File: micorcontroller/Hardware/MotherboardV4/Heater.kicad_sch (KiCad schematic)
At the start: 48 parts, among them IC1 ITS4200S-ME-O, IC10 ITS4200S-ME-O, IC11 ITS4200S-ME-O, IC4 ITS4200S-ME-O, IC6 ITS4200S-ME-O, IC7 ITS4200S-ME-O, IC8 ITS4200S-ME-O, IC9 ITS4200S-ME-O

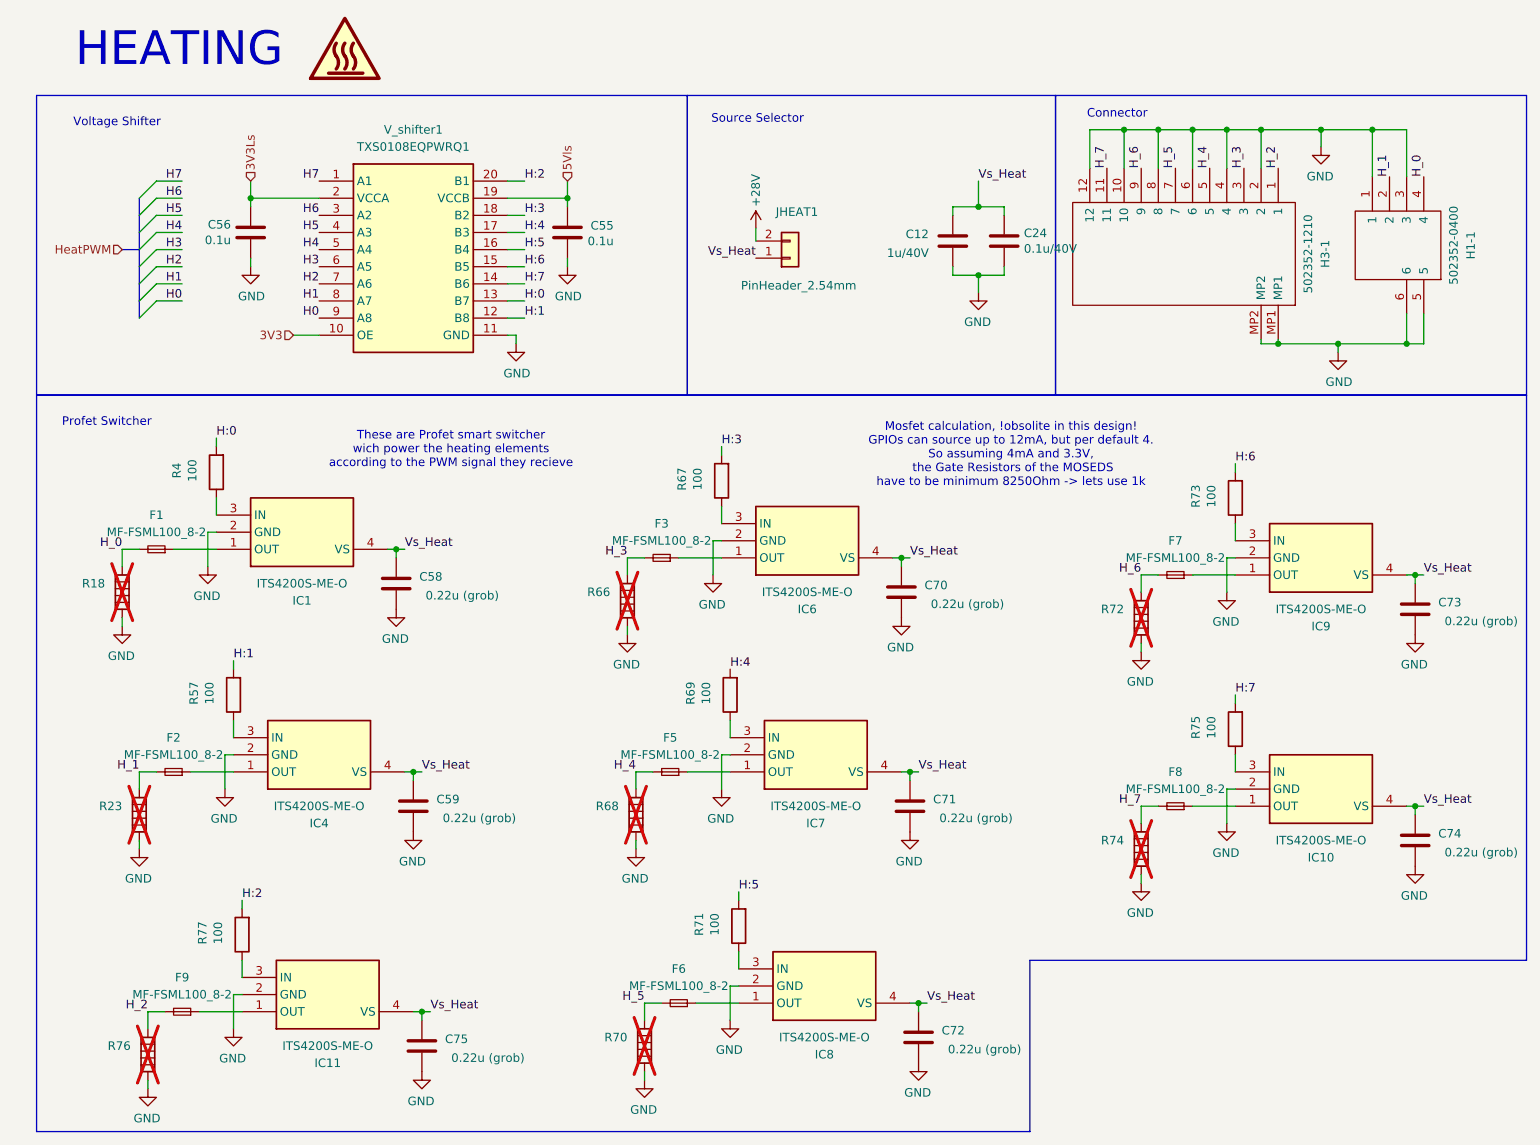
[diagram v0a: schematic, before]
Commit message: added NTC calculation
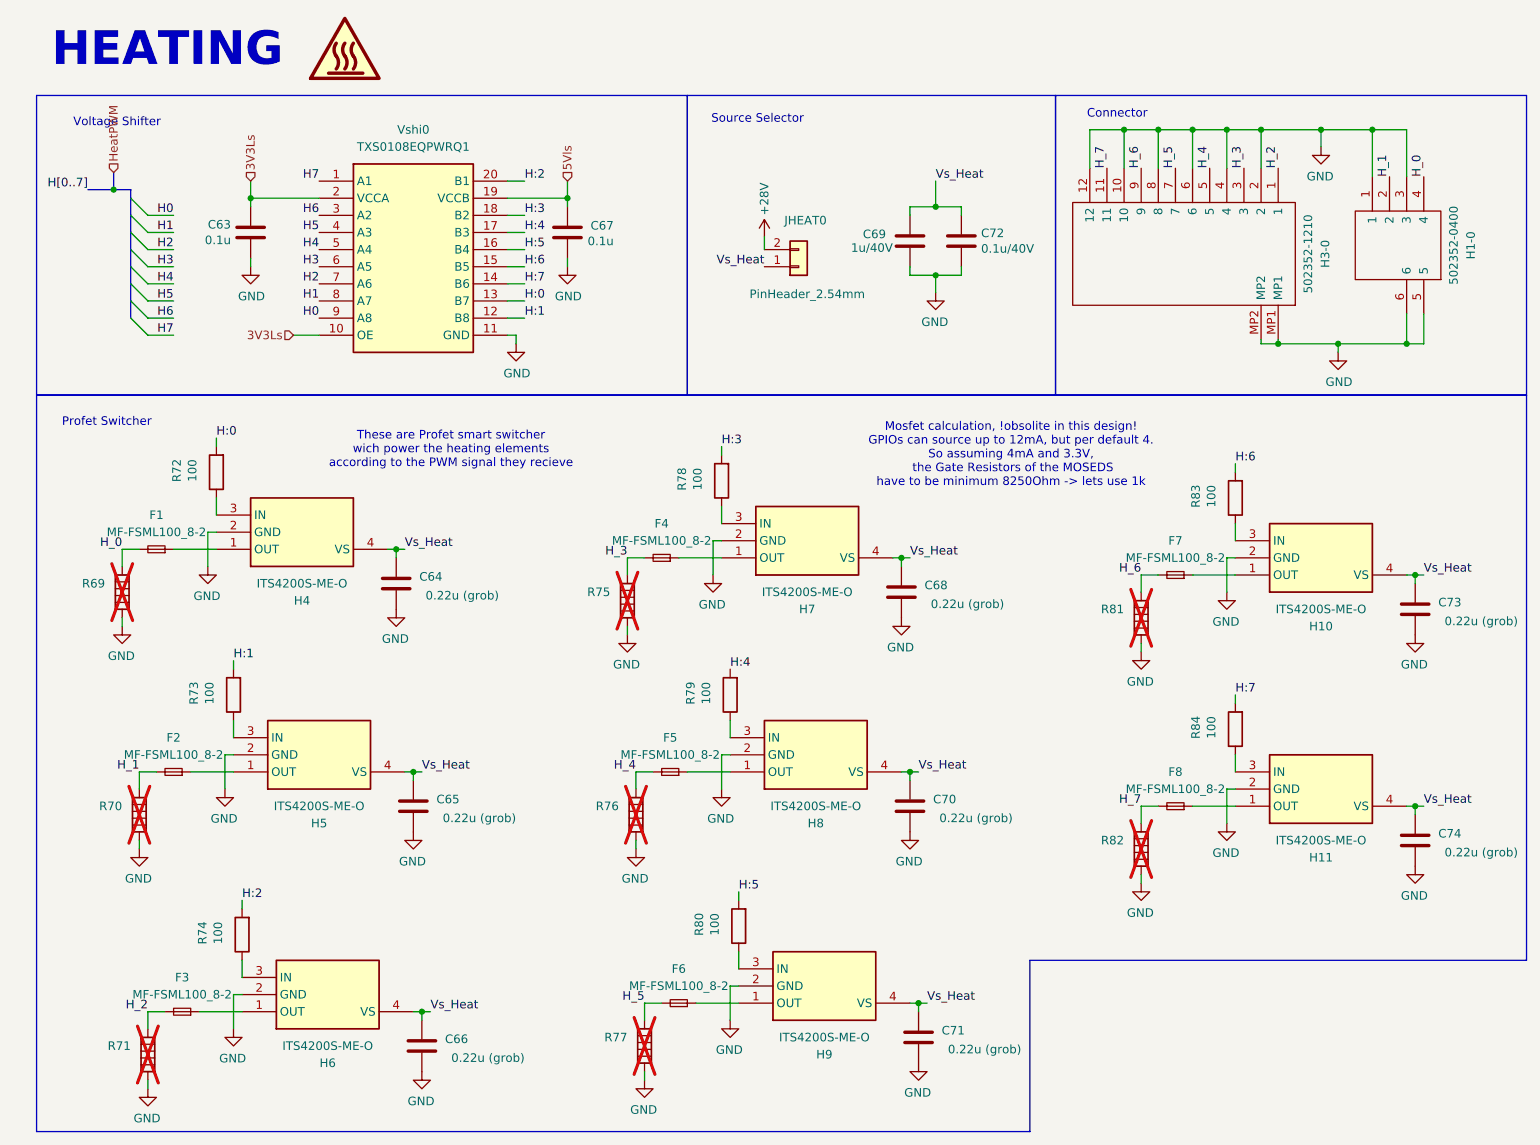
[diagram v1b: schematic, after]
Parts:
- renumbered C56 to C63, C58 to C64, C59 to C65, C75 to C66, C55 to C67, C70 to C68, C12 to C69, C71 to C70, C72 to C71, C24 to C72, F9 to F3, F3 to F4, H1-1 to H1-0, IC9 to H10, IC10 to H11, H3-1 to H3-0, IC1 to H4, IC4 to H5, IC11 to H6, IC6 to H7, IC7 to H8, IC8 to H9, JHEAT1 to JHEAT0, R18 to R69, R23 to R70, R76 to R71, R4 to R72, R57 to R73, R77 to R74, R66 to R75, R68 to R76, R70 to R77, R67 to R78, R69 to R79, R71 to R80, R72 to R81, R74 to R82, R73 to R83, R75 to R84, V_shifter1 to Vshi0
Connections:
- net 3V3 is gone; now on net 3V3Ls: Vshi0.10 (OE)
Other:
- moved on the sheet: C69, C72, JHEAT0

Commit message: added a serial command field for easy debugging
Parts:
- C69: value 1u/40V -> 1u/30V DNP
- C72: value 0.1u/40V -> 0.1u/30V DNP; footprint Capacitor_SMD:C_0402_1005Metric_Pad0.74x0.62mm_HandSolder -> Capacitor_SMD:C_0805_2012Metric_Pad1.18x1.45mm_HandSolder
- renumbered H4 to H0, H5 to H1, H6 to H2, H7 to H3, H8 to H4, H9 to H5, H10 to H6, H11 to H7
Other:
- moved on the sheet: JHEAT0
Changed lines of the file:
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@@
 	)
 	(junction
-		(at 160.02 55.88)
-		(diameter 0)
-		(color 0 0 0 0)
-	)
-	(junction
 		(at 156.21 129.54)
 		(diameter 0)
@@
 	)
 	(junction
+		(at 160.02 58.42)
+		(diameter 0)
+		(color 0 0 0 0)
+	)
+	(junction
 		(at 229.87 66.04)
 		(diameter 0)
@@
 	(wire
 		(pts
-			(xy 160.02 55.88) (xy 156.21 55.88)
+			(xy 160.02 58.42) (xy 156.21 58.42)
 		)
 		(stroke
@@
 	(wire
 		(pts
-			(xy 160.02 58.42) (xy 160.02 55.88)
-		)
-		(stroke
-			(width 0)
-			(type default)
-		)
-	)
-	(wire
-		(pts
 			(xy 64.77 64.77) (xy 68.58 64.77)
 		)
@@
 	(wire
 		(pts
-			(xy 163.83 55.88) (xy 163.83 54.61)
+			(xy 163.83 58.42) (xy 163.83 54.61)
 		)
 		(stroke
@@
 	(wire
 		(pts
-			(xy 163.83 55.88) (xy 160.02 55.88)
+			(xy 163.83 58.42) (xy 160.02 58.42)
 		)
 		(stroke
@@
 	(wire
 		(pts
-			(xy 134.62 50.165) (xy 134.62 52.07)
+			(xy 132.08 47.625) (xy 132.08 49.53)
 		)
 		(stroke
@@
 	(wire
 		(pts
+			(xy 160.02 58.42) (xy 160.02 60.96)
+		)
+		(stroke
+			(width 0)
+			(type default)
+		)
+	)
+	(wire
+		(pts
 			(xy 43.18 176.53) (xy 43.18 175.26)
 		)
@@
 	(wire
 		(pts
-			(xy 156.21 55.88) (xy 156.21 54.61)
+			(xy 156.21 58.42) (xy 156.21 54.61)
 		)
 		(stroke
@@
 	)
 	(label "Vs_Heat"
-		(at 134.62 54.61 180)
+		(at 132.08 52.07 180)
 		(fields_autoplaced yes)
 		(effects
@@
 		(on_board yes)
 		(dnp no)
-		(property "Reference" "H11"
+		(property "Reference" "H7"
 			(at 217.17 142.24 0)
 			(effects
@@
 			(project "BalloonMotherboardV4"
 				(path "/a70d325c-f83f-4714-a2b6-4ef8919d016e/ef45ab9a-94f0-47f5-90d7-9f2f46e21e77"
-					(reference "H11")
+					(reference "H7")
 					(unit 1)
 				)
@@
 		(on_board yes)
 		(dnp no)
-		(property "Reference" "H6"
+		(property "Reference" "H2"
 			(at 69.85 172.72 0)
 			(effects
@@
 			(project "BalloonMotherboardV4"
 				(path "/a70d325c-f83f-4714-a2b6-4ef8919d016e/ef45ab9a-94f0-47f5-90d7-9f2f46e21e77"
-					(reference "H6")
+					(reference "H2")
 					(unit 1)
 				)
@@
 		(dnp no)
 		(property "Reference" "C69"
-			(at 152.654 49.784 0)
+			(at 155.956 48.514 0)
 			(effects
 				(font
@@
 			)
 		)
-		(property "Value" "1u/40V"
-			(at 153.67 51.816 0)
+		(property "Value" "1u/30V DNP"
+			(at 160.782 53.848 0)
 			(effects
 				(font
@@
 		(on_board yes)
 		(dnp no)
-		(property "Reference" "H10"
+		(property "Reference" "H6"
 			(at 217.17 107.95 0)
 			(effects
@@
 			(project "BalloonMotherboardV4"
 				(path "/a70d325c-f83f-4714-a2b6-4ef8919d016e/ef45ab9a-94f0-47f5-90d7-9f2f46e21e77"
-					(reference "H10")
+					(reference "H6")
 					(unit 1)
 				)
@@
 		(on_board yes)
 		(dnp no)
-		(property "Reference" "H4"
+		(property "Reference" "H0"
 			(at 66.04 104.14 0)
 			(effects
@@
 			(project "BalloonMotherboardV4"
 				(path "/a70d325c-f83f-4714-a2b6-4ef8919d016e/ef45ab9a-94f0-47f5-90d7-9f2f46e21e77"
-					(reference "H4")
+					(reference "H0")
 					(unit 1)
 				)
@@
 		(on_board yes)
 		(dnp no)
-		(property "Reference" "H8"
+		(property "Reference" "H4"
 			(at 142.24 137.16 0)
 			(effects
@@
 			(project "BalloonMotherboardV4"
 				(path "/a70d325c-f83f-4714-a2b6-4ef8919d016e/ef45ab9a-94f0-47f5-90d7-9f2f46e21e77"
-					(reference "H8")
+					(reference "H4")
 					(unit 1)
 				)
@@
 		(on_board yes)
 		(dnp no)
-		(property "Reference" "H9"
+		(property "Reference" "H5"
 			(at 143.51 171.45 0)
 			(effects
@@
 			(project "BalloonMotherboardV4"
 				(path "/a70d325c-f83f-4714-a2b6-4ef8919d016e/ef45ab9a-94f0-47f5-90d7-9f2f46e21e77"
-					(reference "H9")
+					(reference "H5")
 					(unit 1)
 				)
@@
 		(on_board yes)
 		(dnp no)
-		(property "Reference" "H7"
+		(property "Reference" "H3"
 			(at 140.97 105.41 0)
 			(effects
@@
 			(project "BalloonMotherboardV4"
 				(path "/a70d325c-f83f-4714-a2b6-4ef8919d016e/ef45ab9a-94f0-47f5-90d7-9f2f46e21e77"
-					(reference "H7")
+					(reference "H3")
 					(unit 1)
 				)
@@
 	(symbol
 		(lib_id "Connector_Generic:Conn_01x02")
-		(at 139.7 54.61 0)
+		(at 137.16 52.07 0)
 		(mirror x)
 		(unit 1)
@@
 		(dnp no)
 		(property "Reference" "JHEAT0"
-			(at 140.716 47.752 0)
+			(at 138.176 45.212 0)
 			(effects
 				(font
@@
 		)
 		(property "Value" "PinHeader_2.54mm"
-			(at 140.97 58.674 0)
+			(at 138.43 56.134 0)
 			(effects
 				(font
@@
 		)
 		(property "Footprint" "Connector_PinHeader_2.54mm:PinHeader_1x02_P2.54mm_Vertical"
-			(at 139.7 54.61 0)
+			(at 137.16 52.07 0)
 			(effects
 				(font
@@
 		)
 		(property "Datasheet" "~"
-			(at 139.7 54.61 0)
+			(at 137.16 52.07 0)
 			(effects
 				(font
@@
 		)
 		(property "Description" "Generic connector, single row, 01x02, script generated (kicad-library-utils/schlib/autogen/connector/)"
-			(at 139.7 54.61 0)
+			(at 137.16 52.07 0)
 			(effects
 				(font
@@
 		(dnp no)
 		(property "Reference" "C72"
-			(at 166.751 49.6316 0)
+			(at 164.846 48.26 0)
 			(effects
 				(font
@@
 			)
 		)
-		(property "Value" "0.1u/40V"
-			(at 166.751 51.943 0)
+		(property "Value" "0.1u/30V DNP"
+			(at 159.258 56.388 0)
 			(effects
 				(font
@@
 			)
 		)
-		(property "Footprint" "Capacitor_SMD:C_0402_1005Metric_Pad0.74x0.62mm_HandSolder"
+		(property "Footprint" "Capacitor_SMD:C_0805_2012Metric_Pad1.18x1.45mm_HandSolder"
 			(at 164.7952 54.61 0)
 			(effects
@@
 		(on_board yes)
 		(dnp no)
-		(property "Reference" "H5"
+		(property "Reference" "H1"
 			(at 68.58 137.16 0)
 			(effects
@@
 			(project "BalloonMotherboardV4"
 				(path "/a70d325c-f83f-4714-a2b6-4ef8919d016e/ef45ab9a-94f0-47f5-90d7-9f2f46e21e77"
-					(reference "H5")
+					(reference "H1")
 					(unit 1)
 				)
@@
 	(symbol
 		(lib_id "power:+28V")
-		(at 134.62 50.165 0)
+		(at 132.08 47.625 0)
 		(unit 1)
 		(exclude_from_sim no)
@@
 		(fields_autoplaced yes)
 		(property "Reference" "#PWR0112"
-			(at 134.62 53.975 0)
+			(at 132.08 51.435 0)
 			(effects
 				(font
@@
 		)
 		(property "Value" "+28V"
-			(at 134.62 46.99 90)
+			(at 132.08 44.45 90)
 			(effects
 				(font
@@
 		)
 		(property "Footprint" ""
-			(at 140.97 48.895 0)
+			(at 138.43 46.355 0)
 			(effects
 				(font
@@
 		)
 		(property "Datasheet" ""
-			(at 140.97 48.895 0)
+			(at 138.43 46.355 0)
 			(effects
 				(font
@@
 		)
 		(property "Description" "Power symbol creates a global label with name \"+28V\""
-			(at 134.62 50.165 0)
+			(at 132.08 47.625 0)
 			(effects
 				(font
@@
 	(symbol
 		(lib_id "power:GND")
-		(at 160.02 58.42 0)
+		(at 160.02 60.96 0)
 		(mirror y)
 		(unit 1)
@@
 		(dnp no)
 		(property "Reference" "#PWR0116"
-			(at 160.02 64.77 0)
+			(at 160.02 67.31 0)
 			(effects
 				(font
@@
 		)
 		(property "Value" "GND"
-			(at 159.893 62.8142 0)
+			(at 159.893 65.3542 0)
 			(effects
 				(font
@@
 		)
 		(property "Footprint" ""
-			(at 160.02 58.42 0)
+			(at 160.02 60.96 0)
 			(effects
 				(font
@@
 		)
 		(property "Datasheet" ""
-			(at 160.02 58.42 0)
+			(at 160.02 60.96 0)
 			(effects
 				(font
@@
 		)
 		(property "Description" "Power symbol creates a global label with name \"GND\" , ground"
-			(at 160.02 58.42 0)
+			(at 160.02 60.96 0)
 			(effects
 				(font

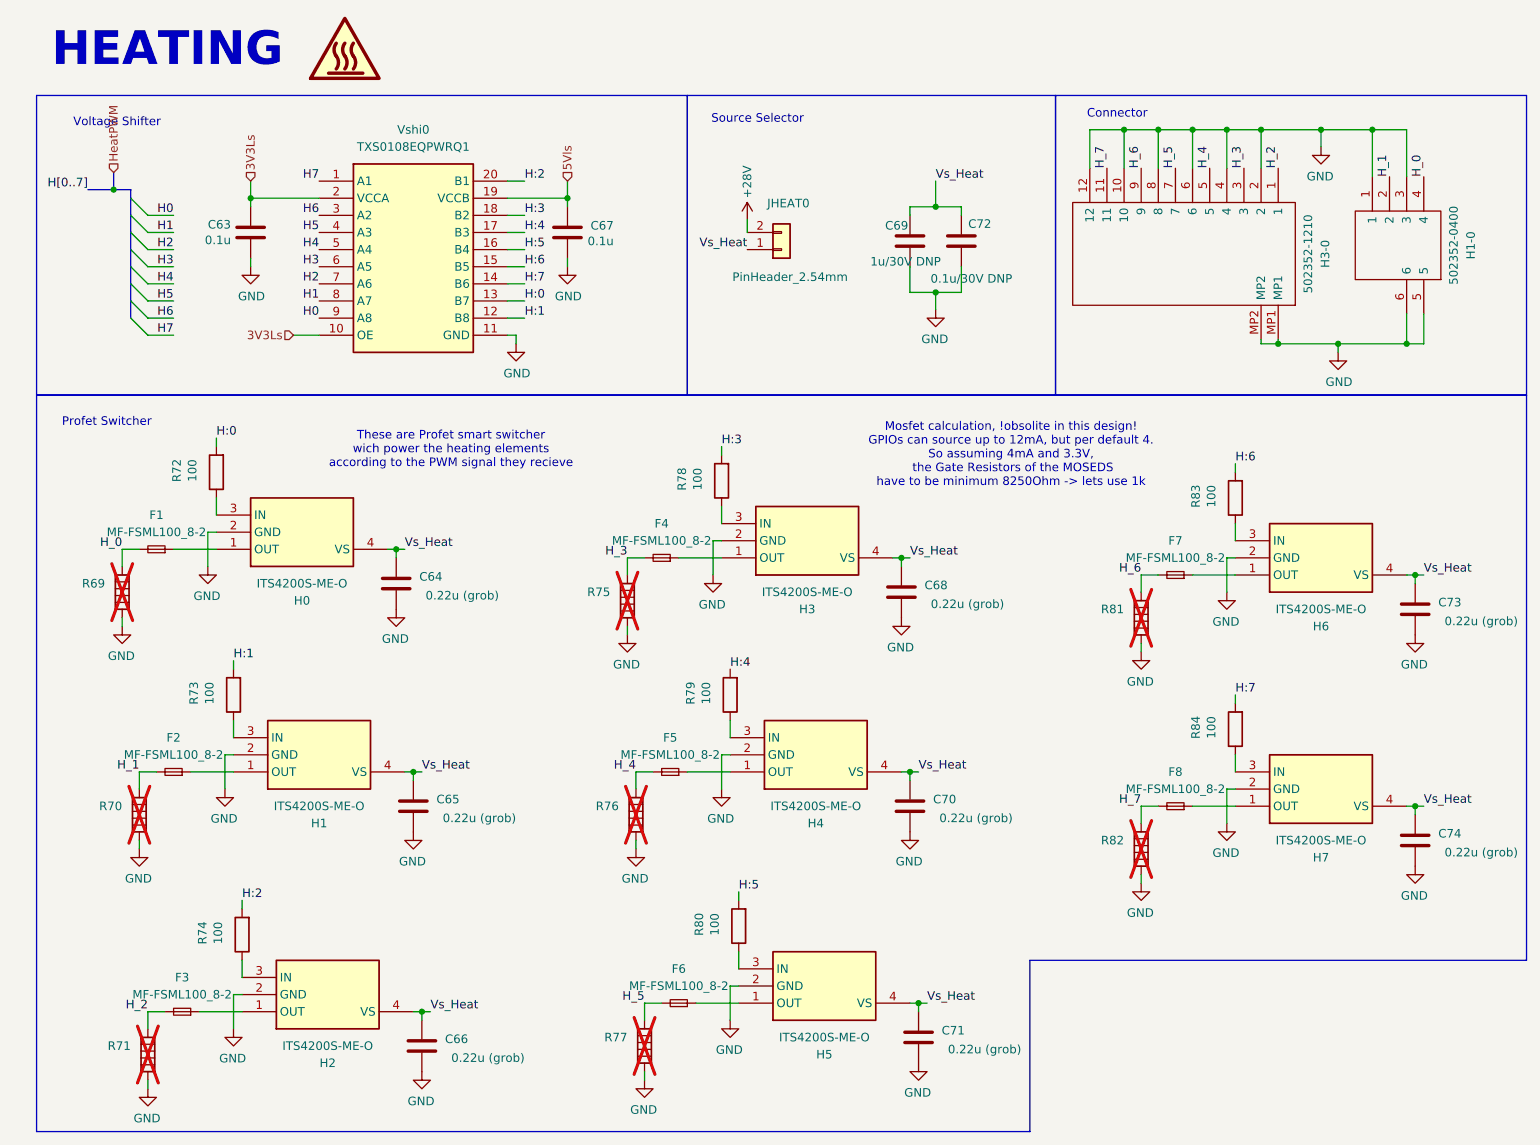
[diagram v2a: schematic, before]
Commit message: Switch to header BASED C file system {headache incomming}
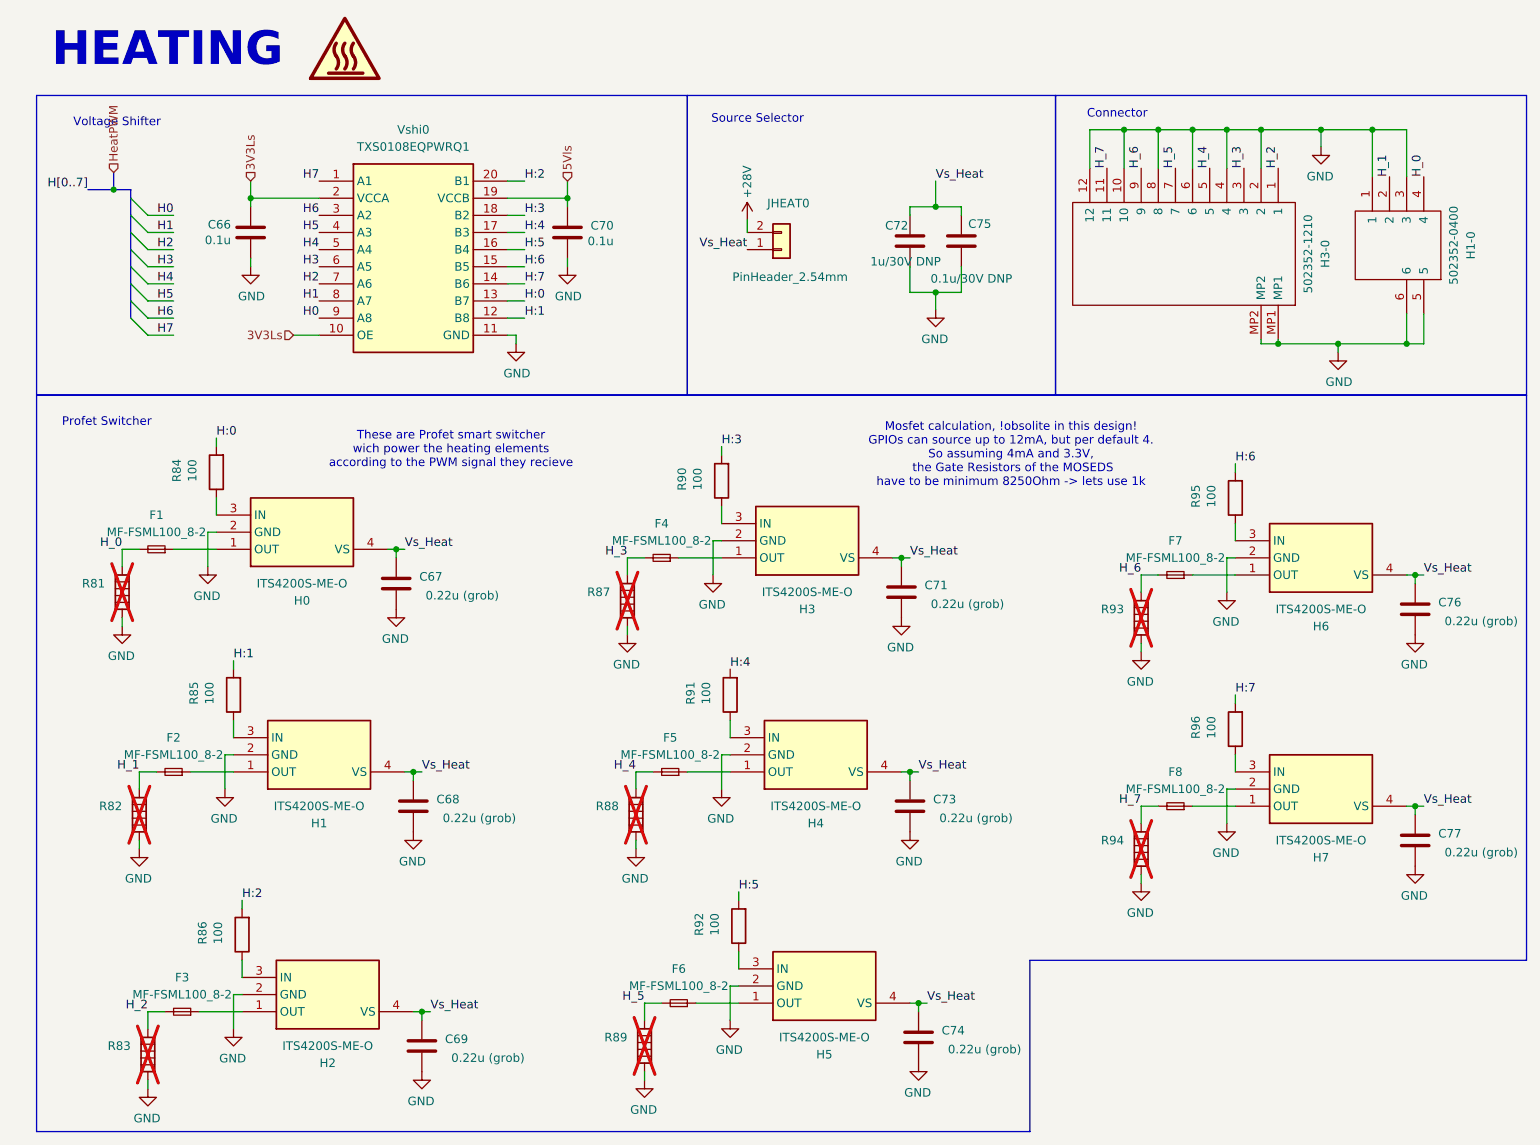
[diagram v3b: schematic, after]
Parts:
- renumbered C63 to C66, C64 to C67, C65 to C68, C66 to C69, C67 to C70, C68 to C71, C69 to C72, C70 to C73, C71 to C74, C72 to C75, C73 to C76, C74 to C77, R69 to R81, R70 to R82, R71 to R83, R72 to R84, R73 to R85, R74 to R86, R75 to R87, R76 to R88, R77 to R89, R78 to R90, R79 to R91, R80 to R92, R81 to R93, R82 to R94, R83 to R95, R84 to R96
